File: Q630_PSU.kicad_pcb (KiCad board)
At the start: 2 copper layers, 99.1 x 50.8 mm, 25 parts, among them J1 ATX PWR, J2 MAC PWR, J3 MAC AUX, J4 FAN1, J5 FAN2, Q1 2N3904, U1 VXO78012

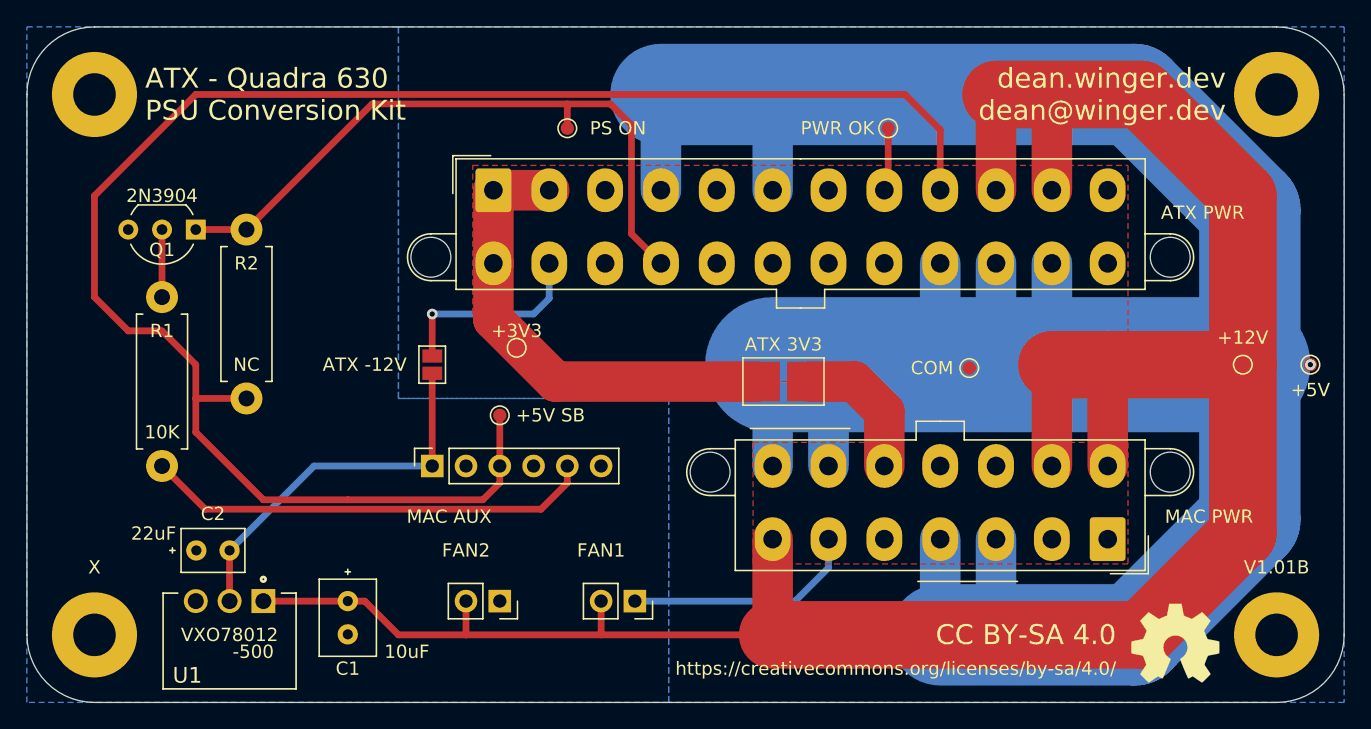
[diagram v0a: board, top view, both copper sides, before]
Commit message: Upgrade project to KiCad 9
- Migrated PCB, schematic, and project files to KiCad 9 format
- Updated global footprint library table with default libraries
- Converted legacy zone fills to modern fill strategy
- Fixed zone priority conflict on B.Cu layer
- Updated Q1 footprint to match current library version
- All DRC checks pass with 0 violations
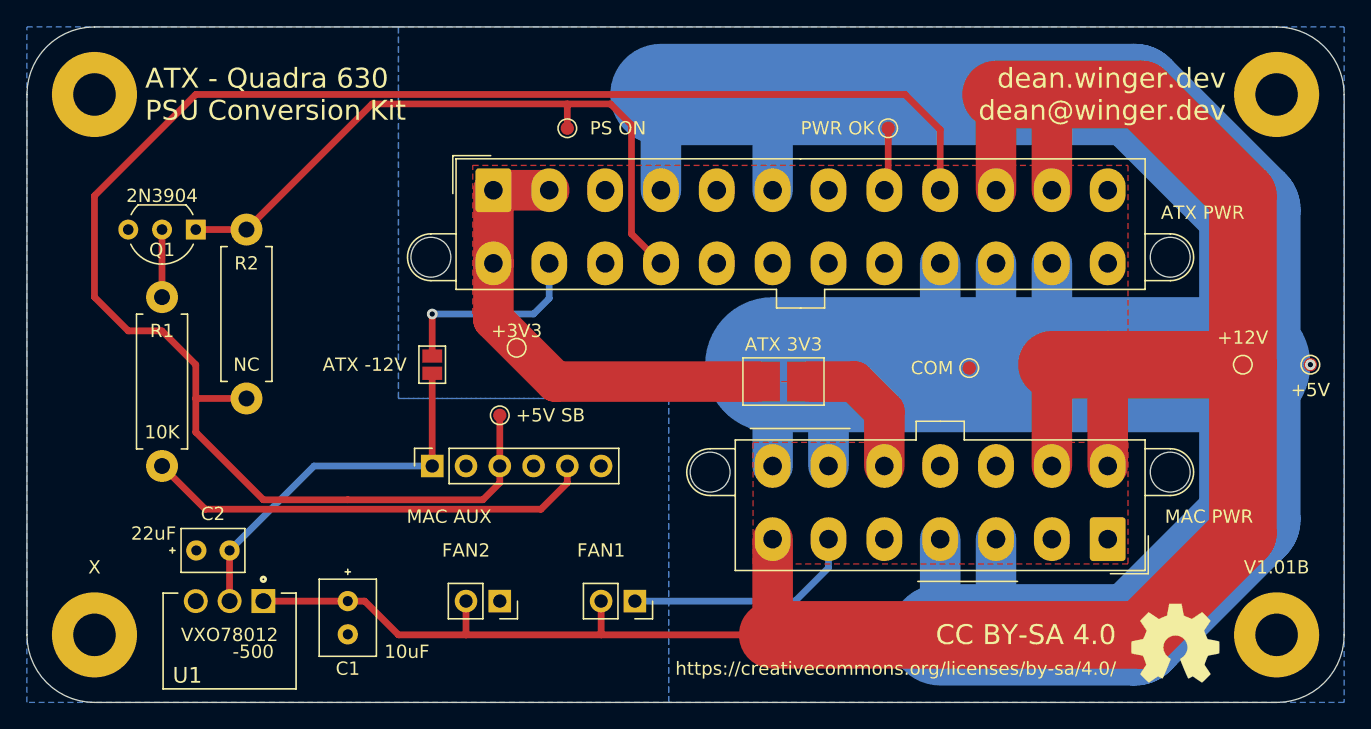
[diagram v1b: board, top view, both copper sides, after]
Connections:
- J1 pad 20: Net-(J1-Pad20) -> unconnected-(J1-Pin_20-Pad20)
- J3 pad 4: Net-(J3-Pad4) -> unconnected-(J3-Pin_4-Pad4)
- J3 pad 6: Net-(J3-Pad6) -> unconnected-(J3-Pin_6-Pad6)
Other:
- net class Default removed
